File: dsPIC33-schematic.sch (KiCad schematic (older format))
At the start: 13 parts, among them IC1 DSPIC33EP64MC502-I_SP, IC2 LM2937ET-3.3_NOPB, J1 Conn_01x05_Male, J2 Conn_01x16_Female, J3 Conn_01x10_Male, J4 Conn_01x03_Male

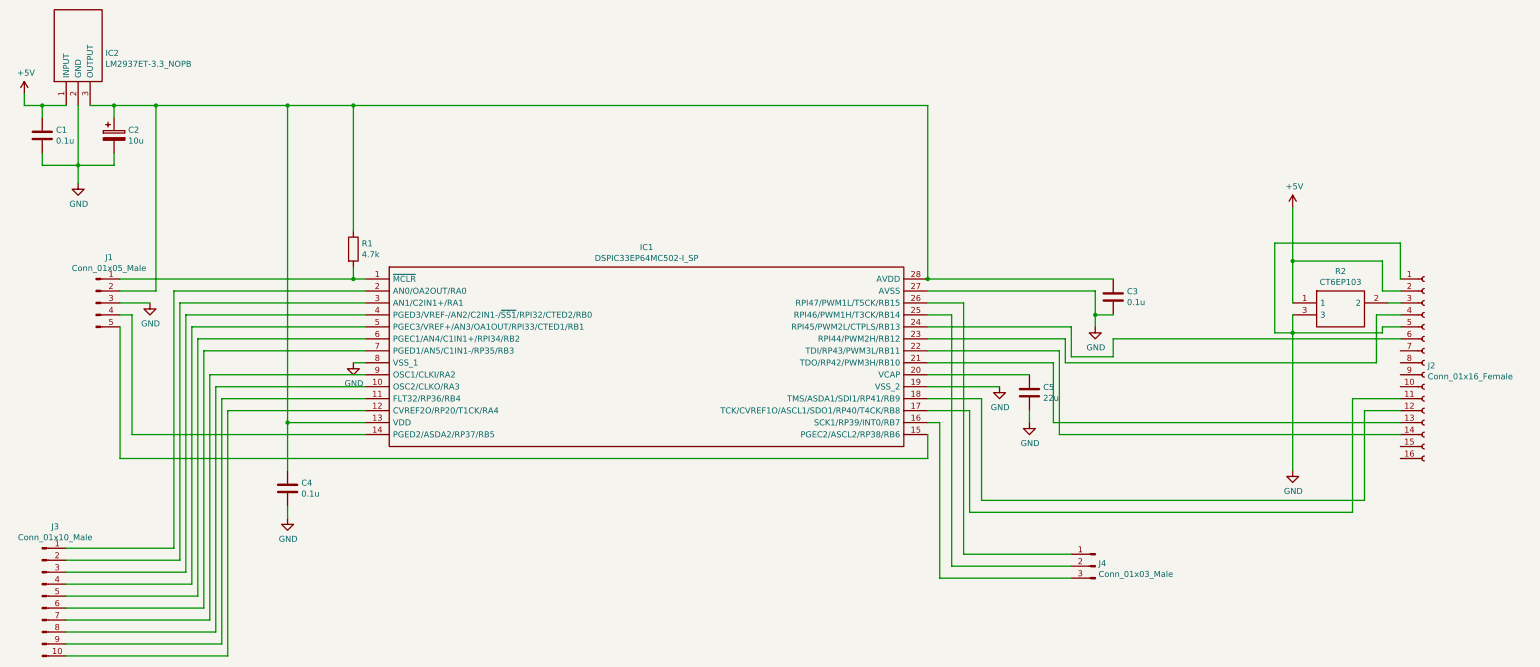
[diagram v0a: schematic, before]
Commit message: updated schematic with netlist
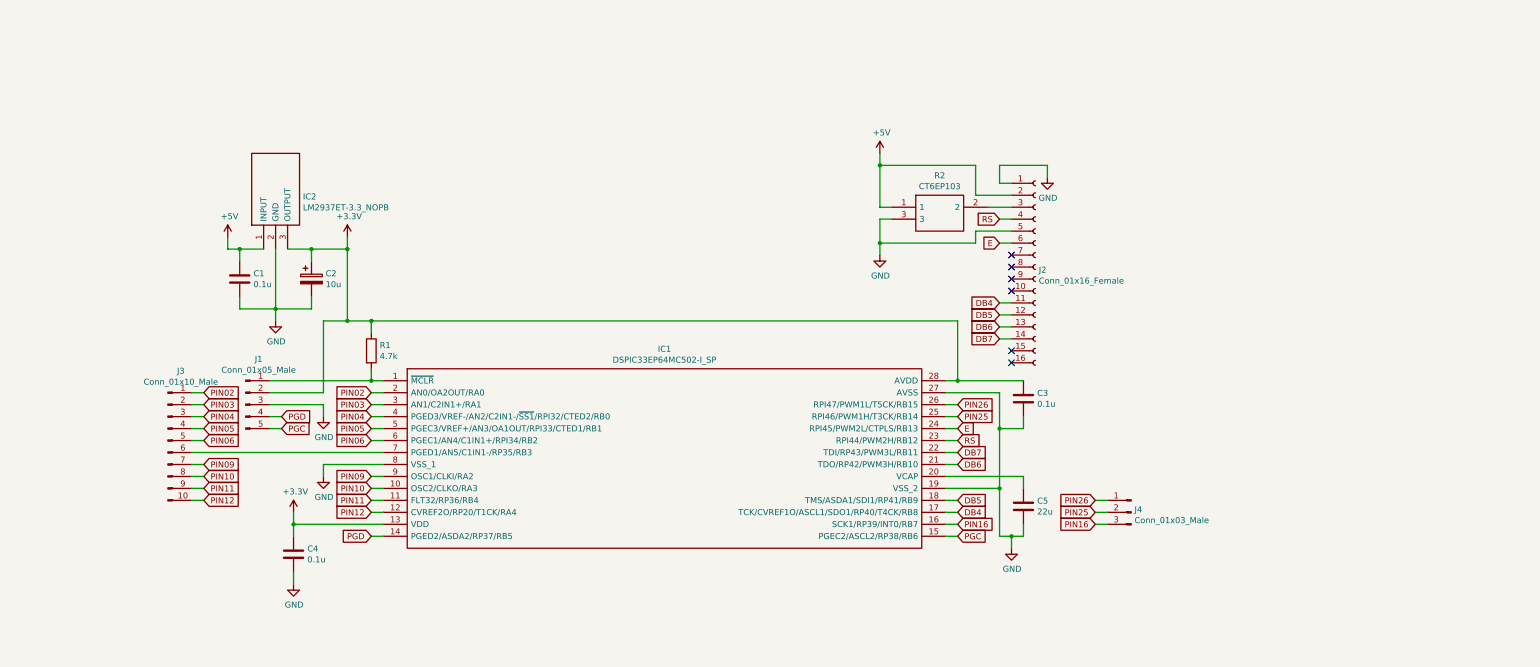
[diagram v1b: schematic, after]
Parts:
- IC1: footprint DIP794W56P254L3486H508Q28N -> DSPIC33EP64MC502-I_SP:DIP794W56P254L3486H508Q28N
- IC2: footprint TO254P470X1028X1955-3P -> LM2937ET-3.3_NOPB:TO254P470X1028X1955-3P
- J2: footprint (none) -> Connector_PinSocket_2.54mm:PinSocket_1x16_P2.54mm_Vertical
- J3: footprint (none) -> Connector_PinSocket_2.54mm:PinSocket_1x10_P2.54mm_Vertical
- J4: footprint (none) -> Connector_PinSocket_2.54mm:PinSocket_1x03_P2.54mm_Vertical
- R2: footprint CT-6EP -> CT6EP103:CT-6EP
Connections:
- net PIN10: now reaches IC1.10 (OSC2/CLKO/RA3), J3.8 (Pin_8)
- net PIN11: now reaches IC1.11 (FLT32/RP36/RB4), J3.9 (Pin_9)
- net PIN12: now reaches IC1.12 (CVREF2O/RP20/T1CK/RA4), J3.10 (Pin_10)
- net +3V3: now reaches C2.1, C3.1, C4.1, IC1.13 (VDD), IC1.28 (AVDD), IC2.3 (OUTPUT), J1.2 (Pin_2), R1.1
- net PGD: now reaches IC1.14 (PGED2/ASDA2/RP37/RB5), J1.4 (Pin_4)
- net PGC: now reaches IC1.15 (PGEC2/ASCL2/RP38/RB6), J1.5 (Pin_5)
- net PIN16: now reaches IC1.16 (SCK1/RP39/INT0/RB7), J4.3 (Pin_3)
- net DB4: now reaches IC1.17 (TCK/CVREF1O/ASCL1/SDO1/RP40/T4CK/RB8), J2.11 (Pin_11)
- net DB5: now reaches IC1.18 (TMS/ASDA1/SDI1/RP41/RB9), J2.12 (Pin_12)
- net PIN02: now reaches IC1.2 (AN0/OA2OUT/RA0), J3.1 (Pin_1)
- net DB6: now reaches IC1.21 (TDO/RP42/PWM3H/RB10), J2.13 (Pin_13)
- net DB7: now reaches IC1.22 (TDI/RP43/PWM3L/RB11), J2.14 (Pin_14)
- net RS: now reaches IC1.23 (RPI44/PWM2H/RB12), J2.4 (Pin_4)
- net E: now reaches IC1.24 (RPI45/PWM2L/CTPLS/RB13), J2.6 (Pin_6)
- net PIN25: now reaches IC1.25 (RPI46/PWM1H/T3CK/RB14), J4.2 (Pin_2)
- net PIN26: now reaches IC1.26 (RPI47/PWM1L/T5CK/RB15), J4.1 (Pin_1)
- net PIN03: now reaches IC1.3 (AN1/C2IN1+/RA1), J3.2 (Pin_2)
- net PIN04: now reaches IC1.4 (PGED3/VREF-/AN2/C2IN1-/~SS1~/RPI32/CTED2/RB0), J3.3 (Pin_3)
- net PIN05: now reaches IC1.5 (PGEC3/VREF+/AN3/OA1OUT/RPI33/CTED1/RB1), J3.4 (Pin_4)
- net PIN06: now reaches IC1.6 (PGEC1/AN4/C1IN1+/RPI34/RB2), J3.5 (Pin_5)
- net PIN09: now reaches IC1.9 (OSC1/CLKI/RA2), J3.7 (Pin_7)
- no-connect marks 0 -> 6
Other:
- moved on the sheet: C1, C2, C3, C4, C5, IC1, IC2, J1, J2, J3, J4, R1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

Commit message: added pcb design
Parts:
- added J5, J6: Conn_01x01, Connector_PinSocket_2.54mm:PinSocket_1x01_P2.54mm_Vertical, symbol Connector_Generic:Conn_01x01
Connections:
- net +5V: now also J5.1 (Pin_1)
- net GND: now also J6.1 (Pin_1)
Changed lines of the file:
@@
 	1    0    0    -1
 $EndComp
+$Comp
+L Connector_Generic:Conn_01x01 J5
+U 1 1 602EB31C
+P 2000 2600
+F 0 "J5" H 1918 2375 50  0000 C CNN
+F 1 "Conn_01x01" H 1918 2466 50  0000 C CNN
+F 2 "Connector_PinSocket_2.54mm:PinSocket_1x01_P2.54mm_Vertical" H 2000 2600 50  0001 C CNN
+F 3 "~" H 2000 2600 50  0001 C CNN
+	1    2000 2600
+	-1   0    0    1
+$EndComp
+Wire Wire Line
+	2200 2600 2300 2600
+Connection ~ 2300 2600
+$Comp
+L Connector_Generic:Conn_01x01 J6
+U 1 1 6030D9A2
+P 2100 3100
+F 0 "J6" H 2018 2875 50  0000 C CNN
+F 1 "Conn_01x01" H 2018 2966 50  0000 C CNN
+F 2 "Connector_PinSocket_2.54mm:PinSocket_1x01_P2.54mm_Vertical" H 2100 3100 50  0001 C CNN
+F 3 "~" H 2100 3100 50  0001 C CNN
+	1    2100 3100
+	-1   0    0    1
+$EndComp
+Wire Wire Line
+	2300 3100 2400 3100
+Connection ~ 2400 3100
 $EndSCHEMATC
